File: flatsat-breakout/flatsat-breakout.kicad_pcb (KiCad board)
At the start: 4 copper layers, 34 x 78.3 mm, 8 parts, among them J1 SFM-120-02-L-DH-TR, J2 61204021621, J3 61204021621, J4 68000-227HLF

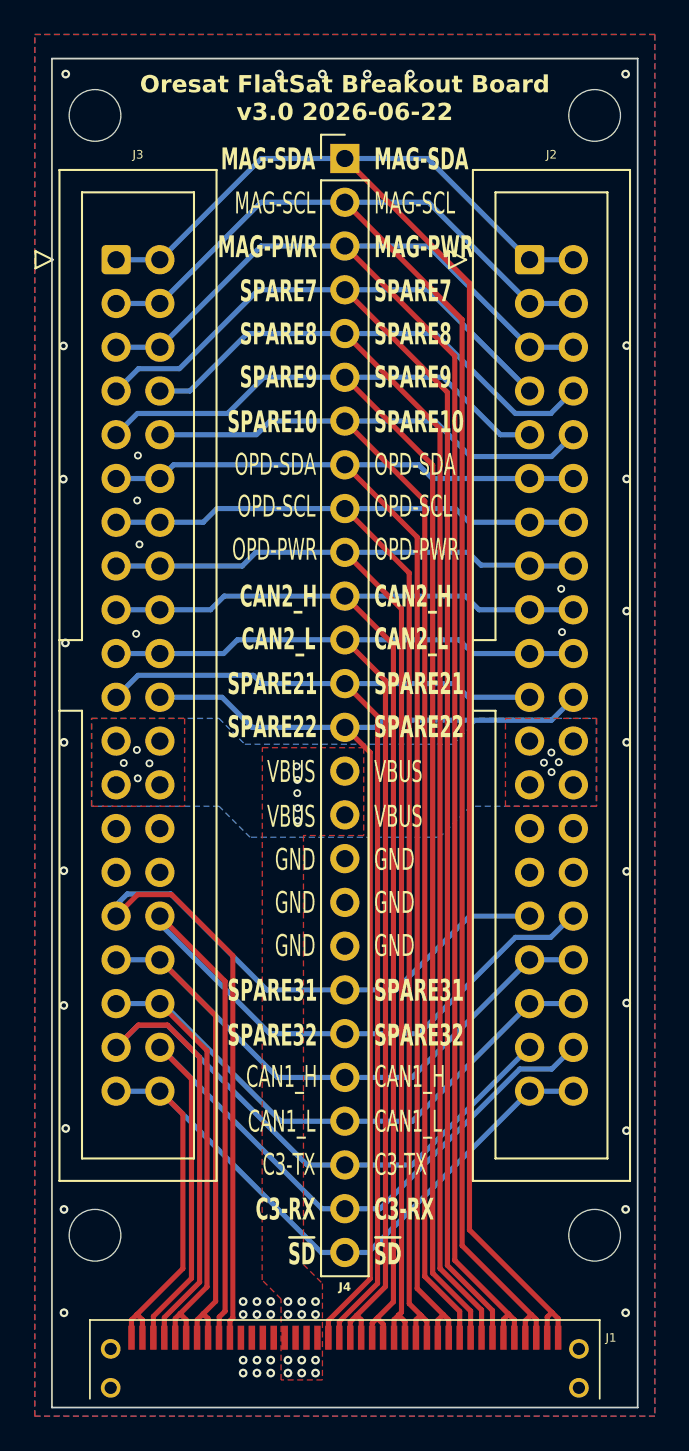
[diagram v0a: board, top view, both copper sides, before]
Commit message: Got rid of aux vs main since we're not doing an aux breakout.
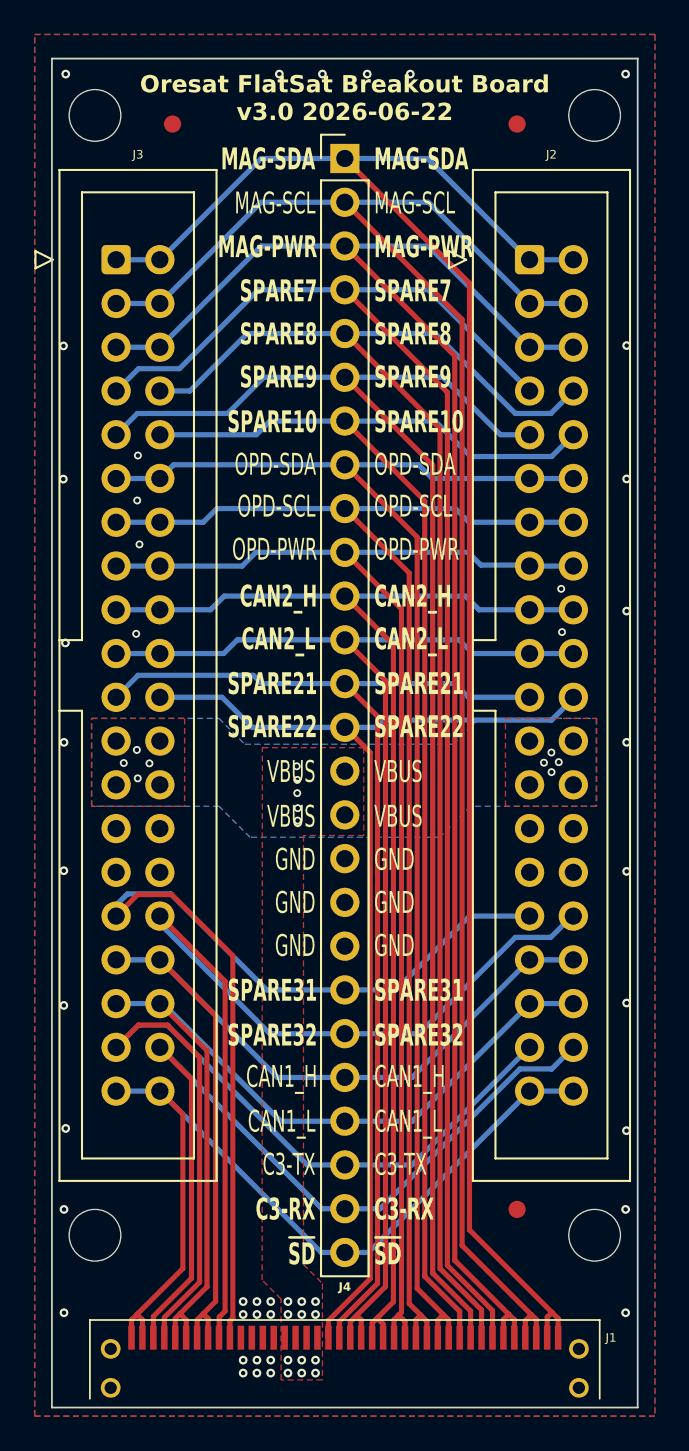
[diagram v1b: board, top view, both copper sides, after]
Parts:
- added REF**: Fiducial_1mm_Mask2mm, Fiducial:Fiducial_1mm_Mask2mm, F.Cu at (160.0, 68.0)
- added REF**: Fiducial_1mm_Mask2mm, Fiducial:Fiducial_1mm_Mask2mm, F.Cu at (160.0, 131.0)
- added REF**: Fiducial_1mm_Mask2mm, Fiducial:Fiducial_1mm_Mask2mm, F.Cu at (140.0, 68.0)
- J4: value 68000-227HLF -> 68000-226HLF
